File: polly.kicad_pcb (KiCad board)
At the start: 2 copper layers, 68.6 x 53.3 mm, 40 parts, among them J5 Conn_02x06_Odd_Even, P1 Power, P2 Analog, P3 Digital, P4 Digital, P5 CONN_01X01, P6 CONN_01X01, P7 CONN_01X01, P8 CONN_01X01, U1 4051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

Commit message: Adjust layout
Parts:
- moved C4 1.27 mm to (127.5, 112.8)
- moved R4 0.25 mm to (169.7, 114.4)
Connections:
- P2 pad 2: +5VA -> /DAC_OUTPUT
- P2 pad 3: /DAC_OUTPUT -> /NOISE
- P2 pad 4: /NOISE -> +5VA
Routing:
- net GND: track 67.5 -> 71.9 mm
- net +5VA: track 87.2 -> 83.6 mm
- net /VCO_CV: track 54.9 -> 58.4 mm
- net VEE: track 99.7 -> 97.7 mm
- net /PWM: track 23.8 -> 25.6 mm
- net /WAVE_SEL: track 30.2 -> 31.8 mm
- net /NOISE: track 9.45 -> 10.6 mm
- net /DAC_OUTPUT: track 19.4 -> 18.3 mm
- net /~VOICE_SEL: track 59.8 -> 58.7 mm
- net /LP_VCA_CV: track 8.74 -> 8.12 mm
- net /MIXER_CV: track 17.1 -> 16.5 mm
- net /CUTOFF: track 43.3 -> 43.8 mm
- net Net-(C4-Pad1): track 5.73 -> 5.20 mm
- added copper zone on F.Cu, net GND
- added copper zone on F.Cu, net GNDA

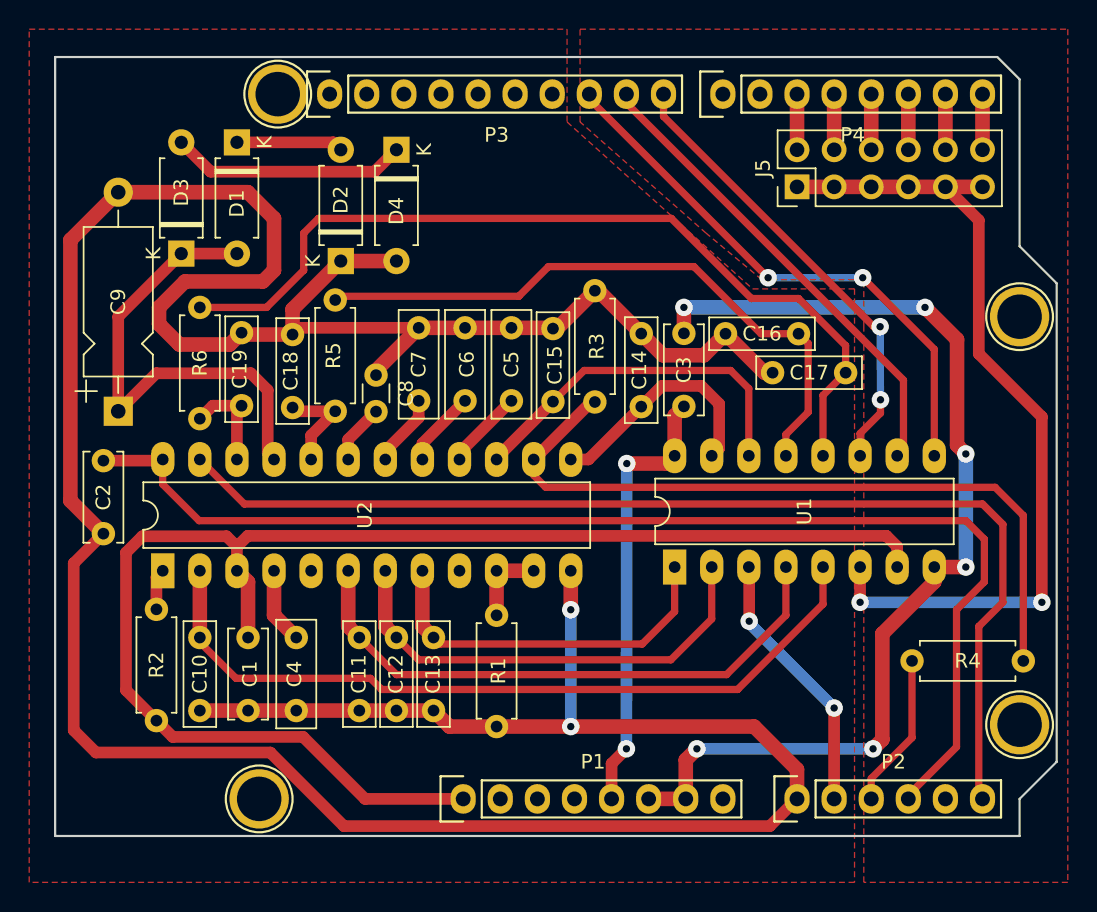
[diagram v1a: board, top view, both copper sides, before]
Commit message: Imporove layout for single sided, add previous versions
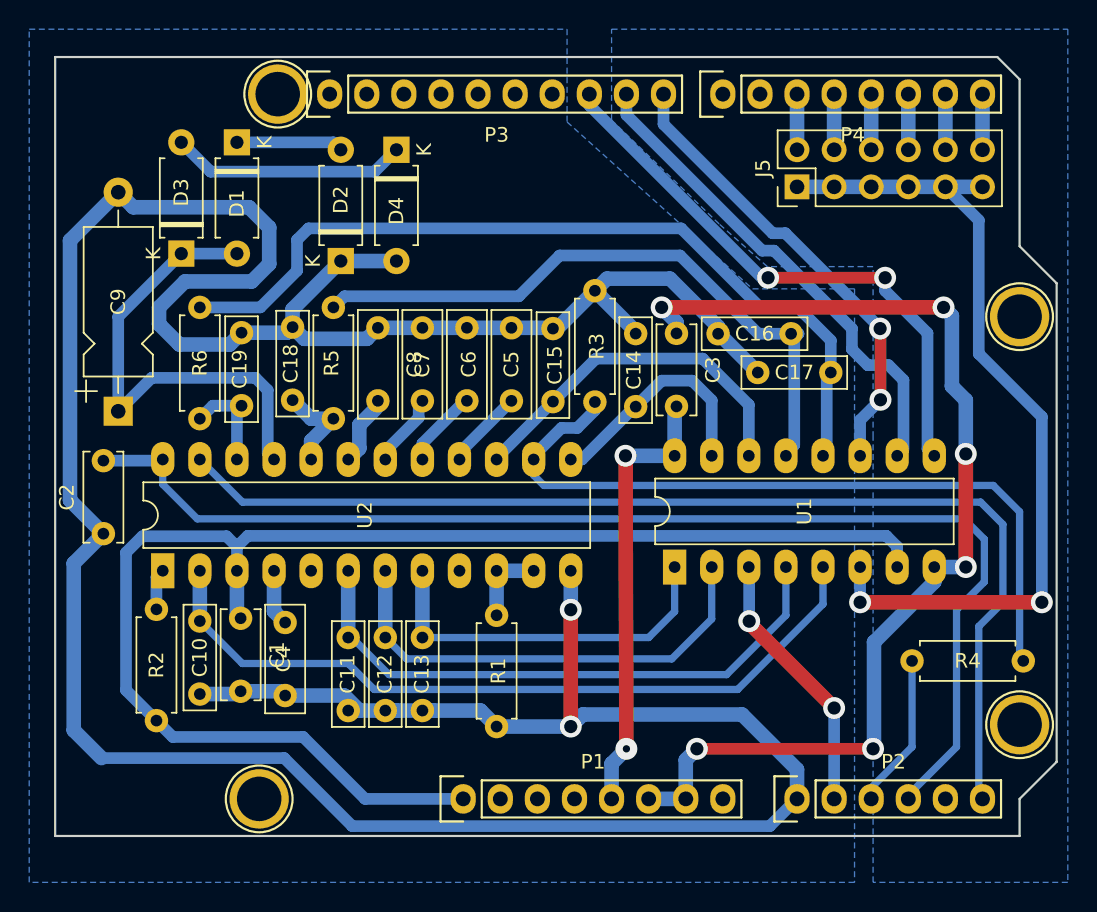
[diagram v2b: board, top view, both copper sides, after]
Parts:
- C18, C19: value 10nF -> 1nF
- C8: footprint Capacitor_THT:C_Disc_D3.0mm_W1.6mm_P2.50mm -> Capacitor_THT:C_Rect_L7.2mm_W2.5mm_P5.00mm_FKS2_FKP2_MKS2_MKP2
- moved C8 3.24 mm to (133.1, 91.6)
- moved C1 1.42 mm to (123.7, 111.5)
- moved C4 1.28 mm to (126.7, 111.7)
- moved C10 1.13 mm to (120.9, 111.6)
- moved C17 1.02 mm to (164.1, 94.6)
- moved C11 0.76 mm to (131.1, 112.8)
- moved C12 0.76 mm to (133.6, 112.8)
- moved C13 0.76 mm to (136.1, 112.8)
- moved R5 0.52 mm to (130.0, 97.8)
- moved C18 0.51 mm to (127.3, 96.5)
- moved C16 0.51 mm to (161.4, 92.0)
- moved C3 0.51 mm to (153.5, 91.9)
- moved C14 0.38 mm to (150.7, 97.0)
- moved C7 0.25 mm to (136.1, 91.6)
- moved C6 0.13 mm to (139.2, 91.6)
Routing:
- net /VCO_CV: track 58.4 -> 53.0 mm
- net GND: track 71.9 -> 74.6 mm
- net /VCA_CV: track 60.0 -> 58.0 mm
- net VEE: track 97.7 -> 96.2 mm
- net Net-(C4-Pad1): track 5.20 -> 3.86 mm
- net /PARAM_SEL_B: track 32.8 -> 34.1 mm
- net /PARAM_SEL_A: track 38.3 -> 39.5 mm
- net /LP_VCA_CV: track 8.12 -> 7.04 mm
- net GNDA: track 235.4 -> 234.5 mm
- net /MOD_AMT: track 40.1 -> 40.8 mm
- added copper zone on B.Cu, net GND
- added copper zone on B.Cu, net GNDA
- removed copper zone on F.Cu, net GND
- removed copper zone on F.Cu, net GNDA

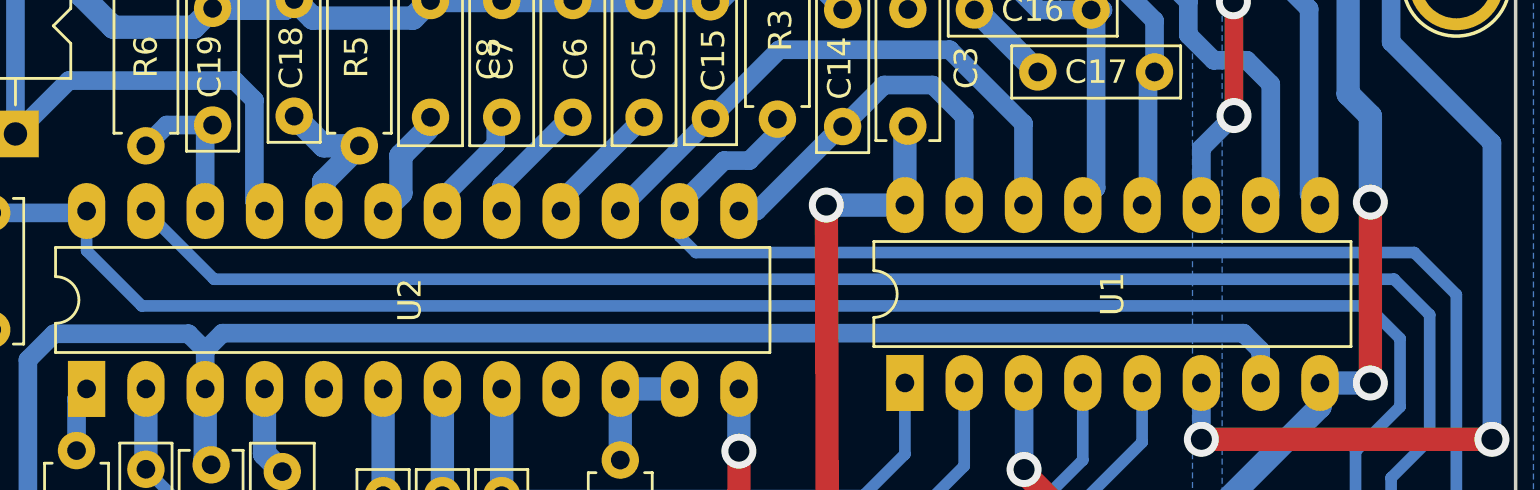
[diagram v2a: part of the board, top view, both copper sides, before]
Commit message: Added smoothing RC to VCF/VCA [just guessing?]
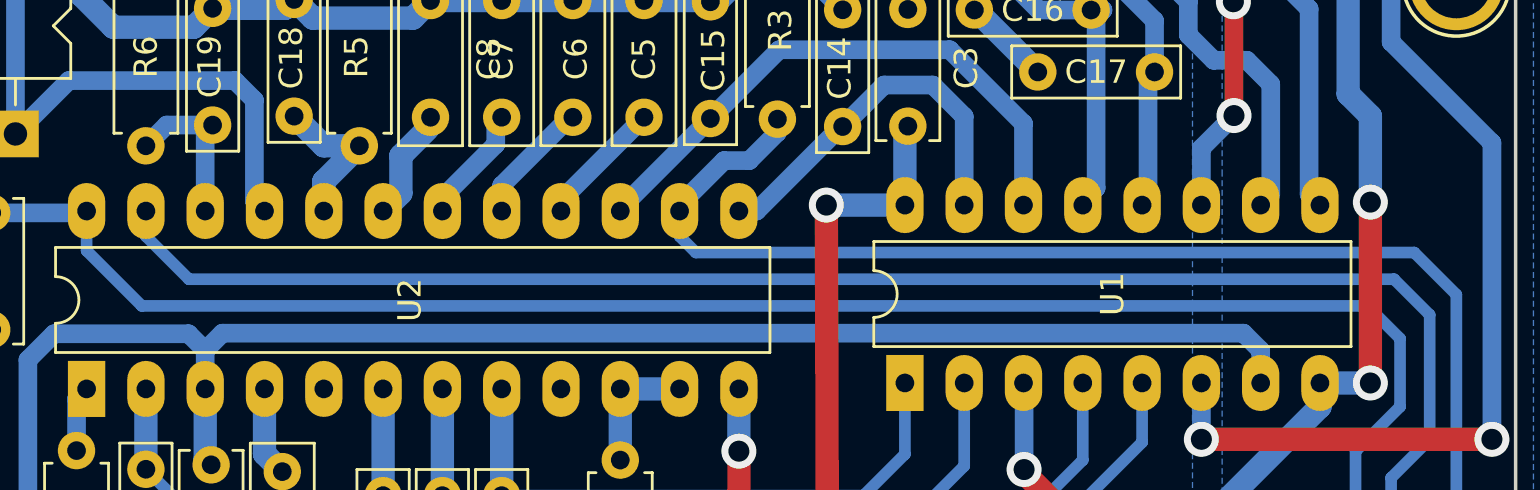
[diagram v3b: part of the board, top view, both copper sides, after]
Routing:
- net /VOICE_OUT: track 76.4 -> 77.0 mm
